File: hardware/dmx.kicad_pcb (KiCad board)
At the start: 4 copper layers, 70 x 70 mm, 63 parts, among them J101 Cortex_Debug, J102 DX07S016JA3, J201 SJ2-25404B-SMT-TR, J301 SJ2-25404B-SMT-TR, SW101 SKSG, SW102 SKSG, U101 TPS78433QWDRBRQ1, U102 ATSAMD51G, U201 THVD2442, U301 TLP2361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

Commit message: Update library
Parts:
- J101: value Cortex_Debug -> Cortex; footprint V2_Cortex_Debug:Cortex_Debug_Pad -> V2_Connector_Debug:Cortex
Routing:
- net GND: vias 102 -> 100
- net +3V3: vias 13 -> 12

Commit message: Use date as revision
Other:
- board text added: "2026-02-07 stencil"

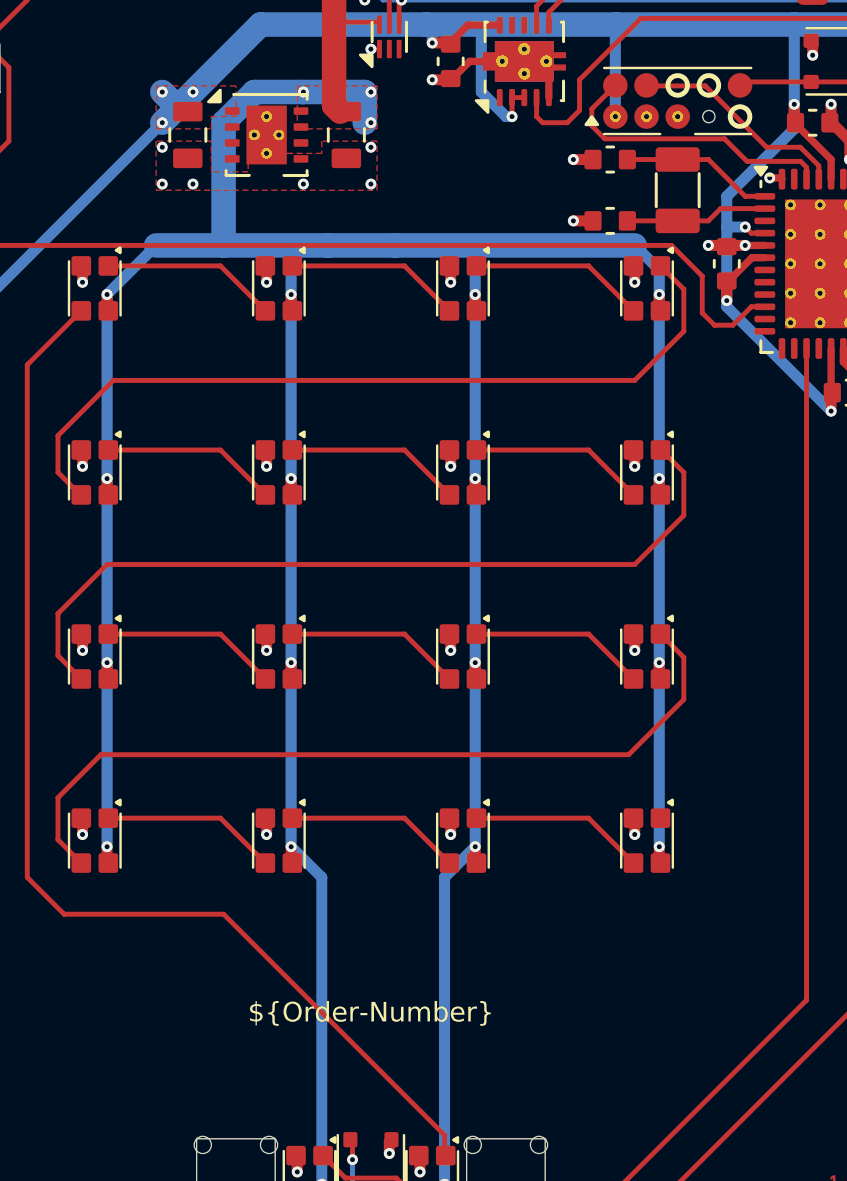
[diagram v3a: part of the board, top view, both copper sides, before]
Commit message: Replace Order_Number
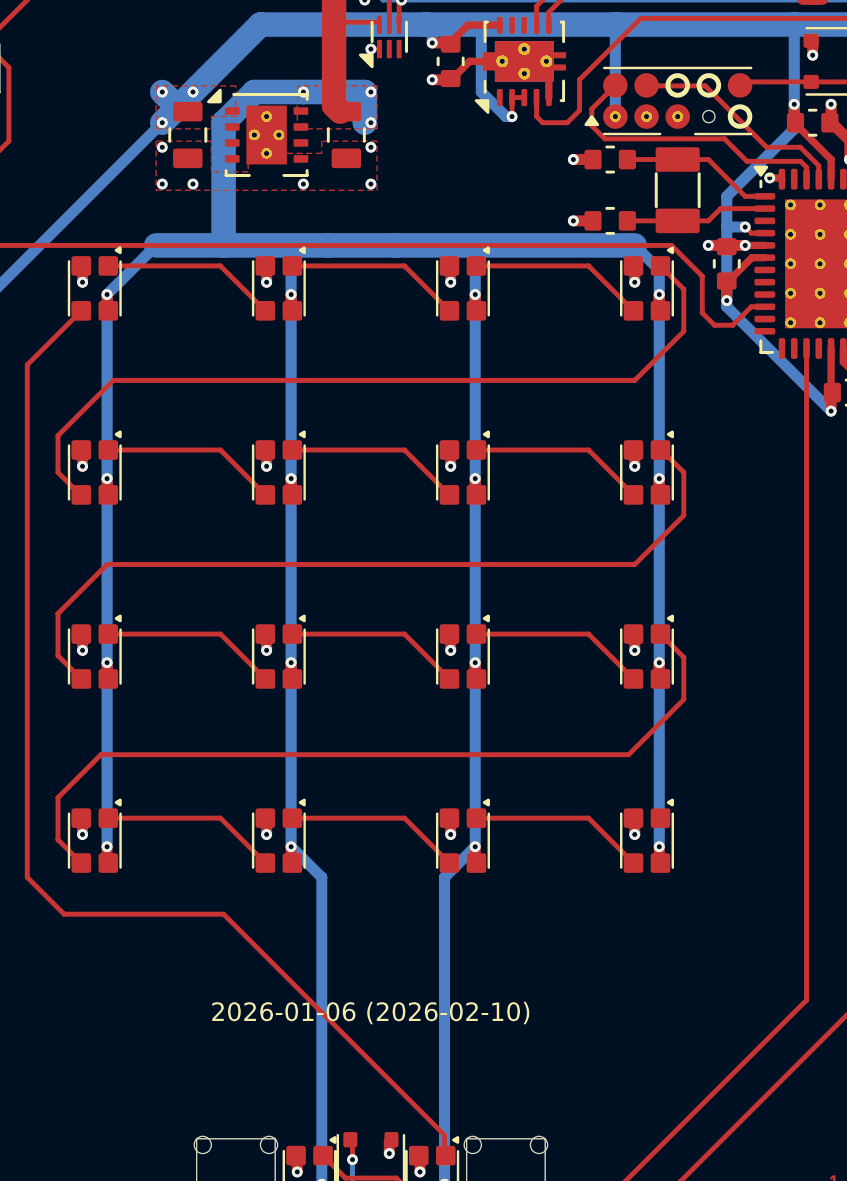
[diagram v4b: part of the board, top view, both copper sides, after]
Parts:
- H101, H102, H103, H104: value MountingHole_2mm -> 2mm
- INFO102: value Order_Number -> ~; footprint V2_Production:Order_Number -> V2_Production:Revision

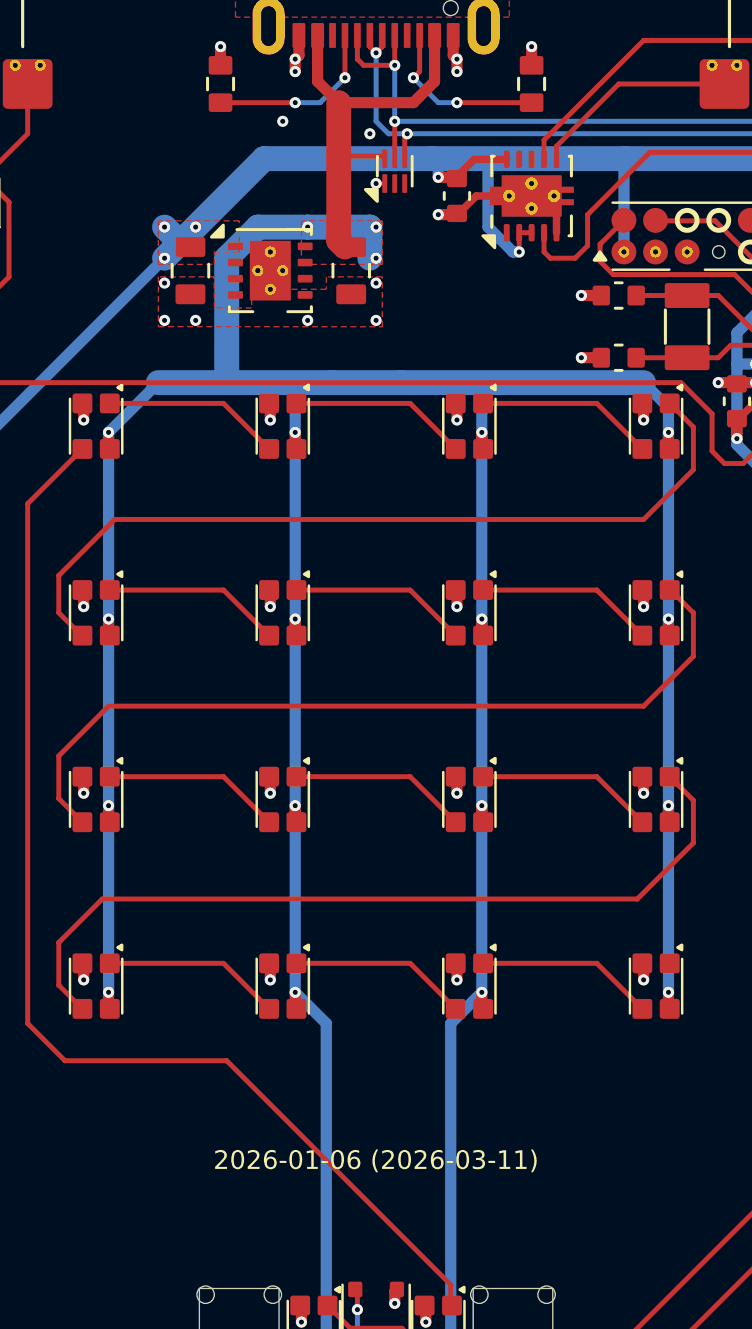
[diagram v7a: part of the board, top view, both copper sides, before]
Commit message: Update ESD suppressor
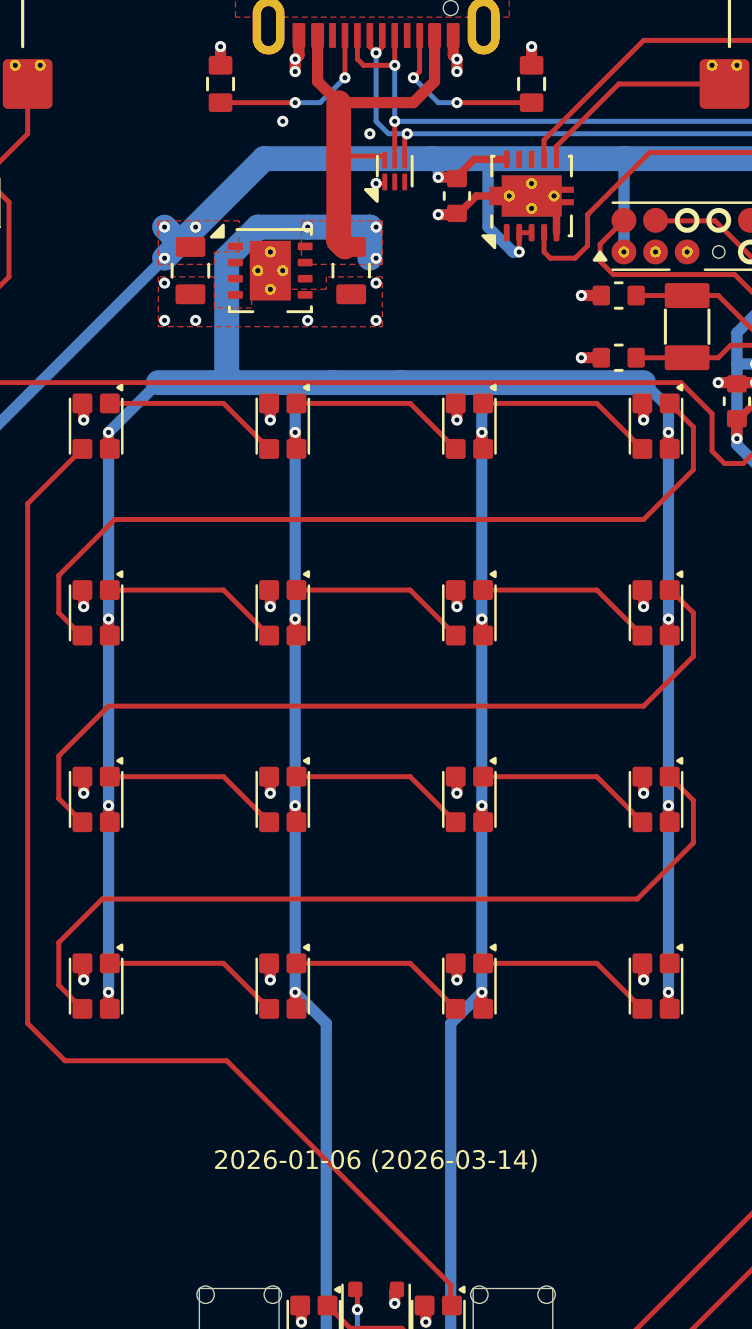
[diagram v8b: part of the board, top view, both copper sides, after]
